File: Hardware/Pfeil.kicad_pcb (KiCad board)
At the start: 4 copper layers, 50 x 9 mm, 61 parts, among them IC1 2536030320001, IC2 nPM1300-CAAA-R, J1 Conn_01x01_Socket, J2 Conn_01x01_Socket, J3 TagConnect, U1 NRF52840-CKAA-R, U2 WSEN-PADS_2511020213301, U3 WSEN-PADS_2511020213301, X1 XTAL 32MHz 8pF, X2 XTAL 32.768kHz 9pF

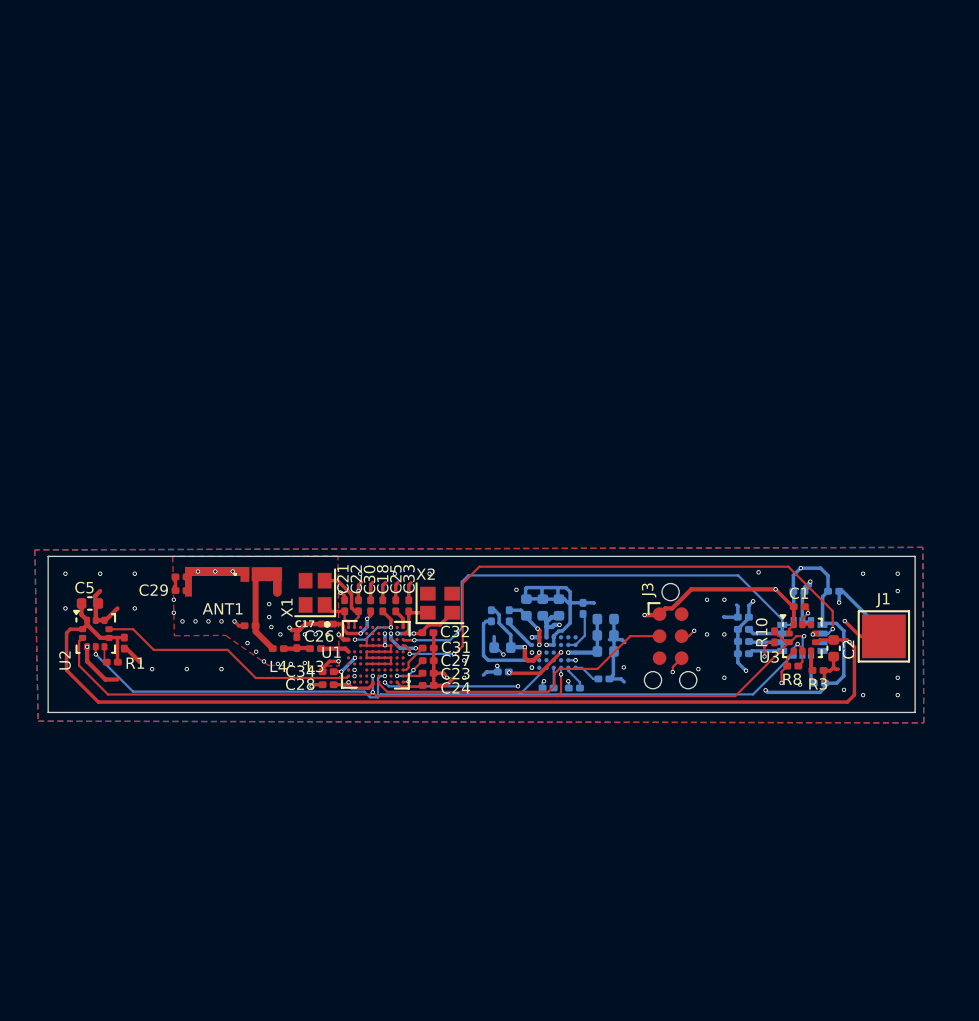
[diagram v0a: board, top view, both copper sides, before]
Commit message: nrf 52840 changing of the package
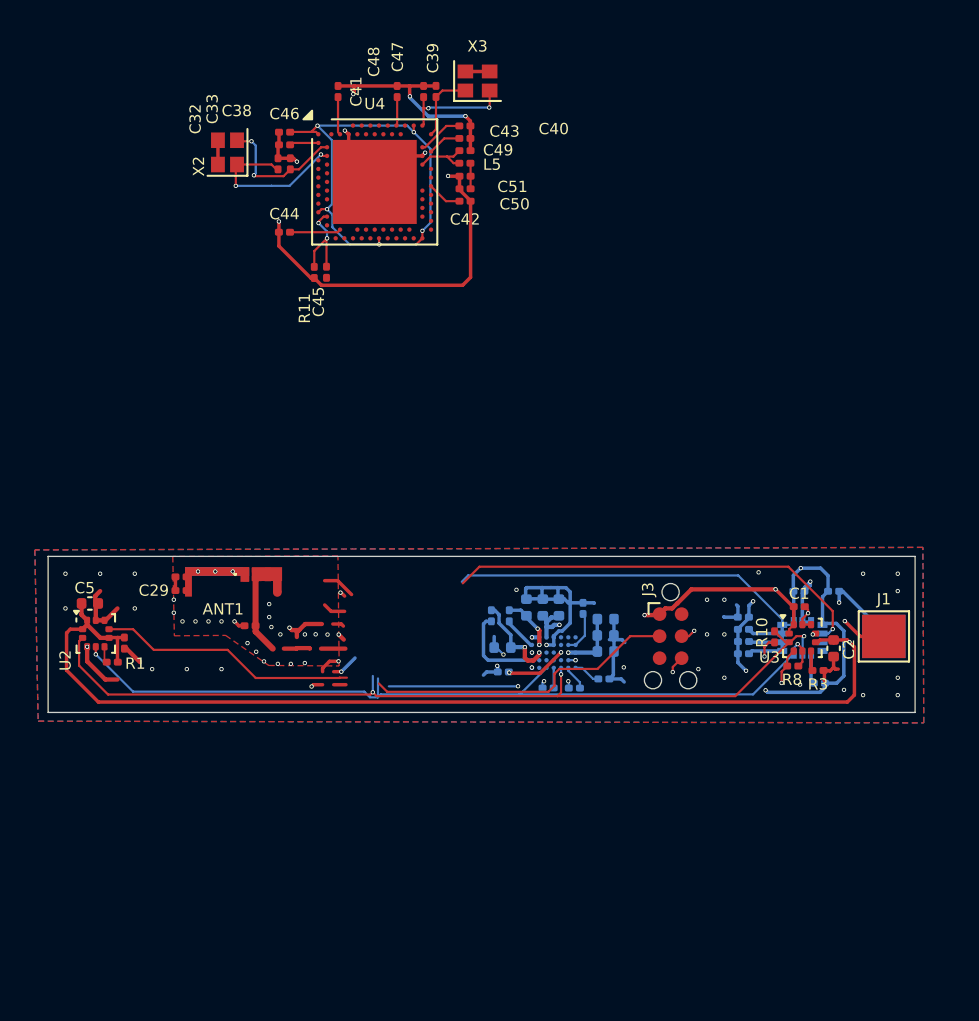
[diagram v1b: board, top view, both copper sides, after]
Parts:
- removed C17, C18: 1uF X7R 10%, Capacitor_SMD:C_0201_0603Metric
- removed C21, C22: 12pF NP0 2%, Capacitor_SMD:C_0201_0603Metric
- removed C23, C24, C31: 4.7uF X7R 10%, Capacitor_SMD:C_0201_0603Metric
- removed C25, C28, C30: 100nF X7R 10%, Capacitor_SMD:C_0201_0603Metric
- removed C26: 1pF 5% 0201, Capacitor_SMD:C_0201_0603Metric
- removed C27: 4.7uF X7S 10%, Capacitor_SMD:C_0201_0603Metric
- removed C34: 820pF X7R 10%, Capacitor_SMD:C_0201_0603Metric
- removed L3: 3.9nH 0201 5%, Inductor_SMD:L_0201_0603Metric
- removed L4: 4.7nH 0201 5%, Inductor_SMD:L_0201_0603Metric
- removed U1: NRF52840-CKAA-R, NRF52840-CKAA-R:BGA94C35P10X10_360X354X51N
- removed X1: XTAL 32MHz 8pF, Crystal:Crystal_SMD_2016-4Pin_2.0x1.6mm
- added C38: 100nF, Capacitor_SMD:C_0201_0603Metric, F.Cu at (138.6, 28.3)
- added C39: N.C., Capacitor_SMD:C_0201_0603Metric, F.Cu at (145.1, 25.2)
- added C40: 100pF, Capacitor_SMD:C_0201_0603Metric, F.Cu at (149.0, 27.2)
- added C41: 1pF, Capacitor_SMD:C_0201_0603Metric, F.Cu at (141.7, 25.2)
- added C42: 820pF, Capacitor_SMD:C_0201_0603Metric, F.Cu at (149.0, 31.5)
- added C43: N.C., Capacitor_SMD:C_0201_0603Metric, F.Cu at (149.0, 27.9)
- added C44: 4.7uF, Capacitor_SMD:C_0201_0603Metric, F.Cu at (138.6, 33.3)
- added C45: 820pF, Capacitor_SMD:C_0201_0603Metric, F.Cu at (140.3, 35.6)
- added C46: 4.7uF, Capacitor_SMD:C_0201_0603Metric, F.Cu at (138.6, 27.5)
- added C47: 12pF NP0 2%, Capacitor_SMD:C_0201_0603Metric, F.Cu at (147.4, 25.2)
- added C48: 12pF NP0 2%, Capacitor_SMD:C_0201_0603Metric, F.Cu at (146.7, 25.2)
- added C49: 100nF, Capacitor_SMD:C_0201_0603Metric, F.Cu at (149.0, 28.6)
- added C50: 100nF, Capacitor_SMD:C_0201_0603Metric, F.Cu at (149.0, 30.8)
- added C51: 100nF, Capacitor_SMD:C_0201_0603Metric, F.Cu at (149.0, 30.1)
- added L5: L, Inductor_SMD:L_0201_0603Metric, F.Cu at (149.0, 29.3)
- added R11: 2R2, Resistor_SMD:R_0201_0603Metric, F.Cu at (141.1, 35.6)
- added U4: nRF52840, Package_DFN_QFN:Nordic_AQFN-73-1EP_7x7mm_P0.5mm, F.Cu at (143.8, 30.4)
- added X3: XTAL 32MHz 8pF, Crystal:Crystal_SMD_2016-4Pin_2.0x1.6mm, F.Cu at (149.8, 24.6)
- moved X2 28.7 mm to (135.3, 28.7), turned to 90 degrees
- moved C32 28.4 mm to (138.3, 29.4), turned to 90 degrees
- moved C33 26.4 mm to (139.0, 29.4)
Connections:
- net VDD renamed /ISDS_INT_00
- C32 pad 1: Net-(U1A-P0.00/XL1) -> Net-(U4-XL2/P0.01)
- C33 pad 2: Net-(U1A-P0.01/XL2) -> Net-(U4-XL1/P0.00)
- X2 pad 1: Net-(U1A-P0.01/XL2) -> Net-(U4-XL2/P0.01)
- X2 pad 2: Net-(U1A-P0.00/XL1) -> Net-(U4-XL1/P0.00)
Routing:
- net GND: track 93.8 -> 123.3 mm, vias 73 -> 71
- net GND VDD NRF: track 0.00 -> 28.1 mm, vias 0 -> 5
- net /ISDS_INT_00: track 99.2 -> 72.4 mm, vias 10 -> 4
- net /SWCLK: track 27.5 -> 16.7 mm, vias 2 -> 1
- net (no net): track 0.00 -> 10.5 mm, vias 0 -> 1
- net Net-(U4-XL2/P0.01): track 0.00 -> 9.43 mm, vias 0 -> 2
- net Net-(U4-XL1/P0.00): track 0.00 -> 7.89 mm, vias 0 -> 2
- net /ISDS_INT_01: track 32.1 -> 24.5 mm, vias 3 -> 1
- net Net-(U4-XC2): track 0.00 -> 6.47 mm, vias 0 -> 2
- net GND VBUS NRF: track 0.00 -> 5.37 mm, vias 0 -> 2
- net Net-(U1C-XC2): track 4.16 -> 0.00 mm
- net Net-(U4-XC1): track 0.00 -> 4.12 mm
- net Net-(U1A-P0.00/XL1): track 3.69 -> 0.00 mm, vias 2 -> 0
- net Net-(U1B-DEC4): track 3.58 -> 0.00 mm, vias 2 -> 0
- net Net-(U4-ANT): track 0.00 -> 3.33 mm
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
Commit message: bigger pcb and no more npm1300
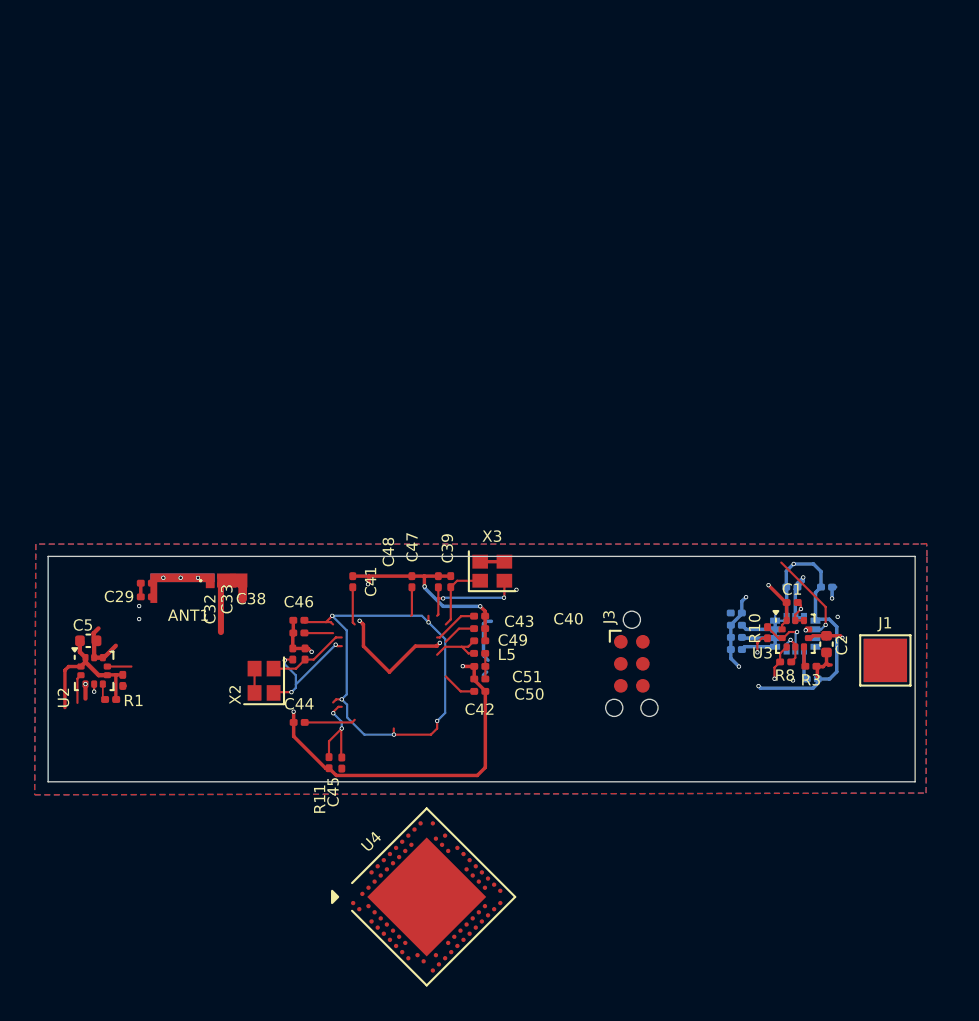
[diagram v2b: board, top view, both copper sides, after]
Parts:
- removed C10: 1.0uF, Capacitor_SMD:C_0201_0603Metric
- removed C11: 1.0uF X5R 10V 10%, Capacitor_SMD:C_0201_0603Metric
- removed C12, C13, C14, C15, C16, C19, C36: 10uF X5R 25V 20%, Capacitor_SMD:C_0402_1005Metric
- removed C37: 100nF X5R 10%, Capacitor_SMD:C_0201_0603Metric
- removed C6: 0.8pF NPO 5%, Capacitor_SMD:C_0201_0603Metric
- removed IC2: nPM1300-CAAA-R, nPM1300-CAAA-R:BGA35C44P7X5_308X238X51
- removed L1, L2: 2.2uH DCR <400mR 20%, Inductor_SMD:L_0201_0603Metric
- removed R12: 47k 1%, Resistor_SMD:R_0201_0603Metric
- removed R13: 270k 1%, Resistor_SMD:R_0201_0603Metric
- moved U4 41.3 mm to (146.8, 71.6), turned to 45 degrees
- moved X2 30.5 mm to (137.5, 59.2)
- moved R11 28.3 mm to (141.9, 63.9)
- moved C32 28.3 mm to (139.1, 57.6)
- moved C50 28.3 mm to (149.9, 59.1)
- moved C51 28.3 mm to (149.9, 58.3)
- moved C33 28.3 mm to (139.8, 57.6)
- moved C42 28.3 mm to (149.9, 59.8)
- moved C44 28.3 mm to (139.5, 61.6)
- moved C45 28.3 mm to (141.2, 63.9)
- moved X3 28.3 mm to (150.6, 52.9)
- moved C39 28.3 mm to (146.0, 53.5)
- moved C40 28.3 mm to (149.9, 55.4)
- moved C41 28.3 mm to (142.6, 53.5)
- moved C43 28.3 mm to (149.9, 56.2)
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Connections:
- C46 pad 2: GND VDD NRF -> GND
- R11 pad 2: GND VBUS -> GND
- U4 pad A22: GND VDD NRF -> GND
- U4 pad AD14: GND VDD NRF -> GND
- U4 pad AD23: GND VDD NRF -> GND
- U4 pad B1: GND VDD NRF -> GND
- U4 pad W1: GND VDD NRF -> GND
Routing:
- net /I2C_SCL: track 98.8 -> 7.42 mm, vias 5 -> 3
- net +3V3: track 88.9 -> 22.7 mm, vias 4 -> 2
- net /ISDS_INT_00: track 72.4 -> 35.3 mm
- net GND VDD NRF: track 28.1 -> 0.00 mm, vias 5 -> 0
- net /PADS_INT02: track 26.0 -> 3.63 mm, vias 2 -> 1
- net /SWDIO: track 20.0 -> 0.00 mm, vias 1 -> 0
- net /VBAT: track 19.5 -> 0.00 mm, vias 2 -> 0
- net /RESET: track 18.1 -> 0.00 mm
- net /ISDS_INT_01: track 24.5 -> 6.75 mm
- net /SWCLK: track 16.7 -> 0.00 mm, vias 1 -> 0
- net /PADS_INT01: track 14.9 -> 1.39 mm
- net GND: track 123.3 -> 113.6 mm, vias 71 -> 24
- net (no net): track 10.5 -> 1.40 mm, vias 1 -> 0
- net Net-(IC2-PVDD): track 6.12 -> 0.00 mm, vias 2 -> 0
- net /3.0V: track 5.45 -> 0.00 mm, vias 2 -> 0
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- added copper zone on B.Cu, net (none)
- added copper zone on F.Cu, net (none)
- added copper zone on In1.Cu, net (none)
- added copper zone on In2.Cu, net (none)
- removed copper zone on B.Cu, net GND
- removed copper zone on F.Cu, net GND
- removed copper zone on In1.Cu, net GND
- removed copper zone on In2.Cu, net GND
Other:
- board size 50 x 9 mm -> 50 x 13 mm

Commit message: start ing to routing with the new pcb
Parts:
- removed J1, J2: Conn_01x01_Socket, TestPoint:TestPoint_Pad_2.5x2.5mm
- added C10: 1uF, Capacitor_SMD:C_0201_0603Metric, F.Cu at (161.1, 61.8)
- added C11: 1uF, Capacitor_SMD:C_0201_0603Metric, F.Cu at (161.1, 62.5)
- added C12: 1uF, Capacitor_SMD:C_0201_0603Metric, F.Cu at (165.8, 61.4)
- added C6: 0.8pF NPO 5%, Capacitor_SMD:C_0201_0603Metric, F.Cu at (153.2, 56.2)
- added IC2: AP7312-1233FM-7, LIB_AP7312-1233FM-7:SON50P201X181X60-7N, F.Cu at (163.4, 62.0)
- moved ANT1 18.6 mm to (153.6, 53.5)
- moved C29 18.6 mm to (149.2, 54.4)
- moved C4 18.6 mm to (149.2, 53.6)
- moved NT1 18.6 mm to (154.8, 54.0)
- moved U4 15.1 mm to (139.3, 58.6)
- moved C48 10.4 mm to (137.1, 53.5), turned to 135 degrees
- moved C39 9.43 mm to (136.6, 54.0), turned to -45 degrees
- moved C41 8.80 mm to (134.2, 56.3), turned to -45 degrees
- moved X3 7.93 mm to (142.7, 53.8), turned to -45 degrees
- moved C47 7.17 mm to (141.1, 52.9), turned to 45 degrees
- moved C38 7.07 mm to (133.3, 59.9), turned to 45 degrees
- moved C33 6.44 mm to (134.2, 60.8), turned to 45 degrees
- moved C40 6.33 mm to (143.6, 55.4), turned to -135 degrees
- moved C42 6.29 mm to (144.6, 56.4), turned to -135 degrees
- moved X2 5.91 mm to (132.7, 62.7), turned to 135 degrees
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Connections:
- C50 pad 1: Net-(C50-Pad1) -> /FEEL
- C51 pad 1: Net-(C50-Pad1) -> /FEEL
- IC1 pad 13: /I2C_SCL -> /I2C_SCL 
- IC1 pad 14: /I2C_SCL -> /I2C_SDA
- L5 pad 1: Net-(C50-Pad1) -> /FEEL
- R8 pad 2: /I2C_SCL -> /I2C_SDA
- U2 pad 2: /I2C_SCL -> /I2C_SCL 
- U2 pad 4: /I2C_SCL -> /I2C_SDA 
- U3 pad 2: /I2C_SCL -> /I2C_SCL 
- U3 pad 4: /I2C_SCL -> /I2C_SDA 
- U4 pad AA24: unconnected-(U4-SWDCLK-PadAA24) -> /SWCLK
- U4 pad AC13: unconnected-(U4-P0.18/~{RESET}-PadAC13) -> /RESET
- U4 pad AC21: unconnected-(U4-P0.25-PadAC21) -> /I2C_SDA 
- U4 pad AC24: unconnected-(U4-SWDIO-PadAC24) -> /SWDIO
- U4 pad G1: unconnected-(U4-P0.26-PadG1) -> /I2C_SCL 
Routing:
- net /I2C_SDA : track 0.00 -> 26.5 mm, vias 0 -> 2
- net /ISDS_INT_00: track 35.3 -> 15.4 mm, vias 4 -> 0
- net GND: track 113.6 -> 95.5 mm, vias 24 -> 12
- net /SWDIO: track 0.00 -> 14.6 mm
- net /SWCLK: track 0.00 -> 14.5 mm
- net /RESET: track 0.00 -> 14.1 mm, vias 0 -> 2
- net /I2C_SCL : track 0.00 -> 12.0 mm, vias 0 -> 2
- net /I2C_SDA: track 0.00 -> 11.2 mm, vias 0 -> 3
- net /FEEL: track 4.47 -> 14.4 mm
- net +3V3: track 22.7 -> 13.2 mm, vias 2 -> 0
- net /I2C_SCL: track 7.42 -> 0.00 mm, vias 3 -> 0
- net /ISDS_INT_01: track 6.75 -> 0.00 mm, vias 1 -> 0
- net /PADS_INT02: track 3.63 -> 0.00 mm, vias 1 -> 0
- net /SW2: track 2.72 -> 0.00 mm
- net Net-(U4-XL2/P0.01): track 7.36 -> 4.93 mm, vias 3 -> 0
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
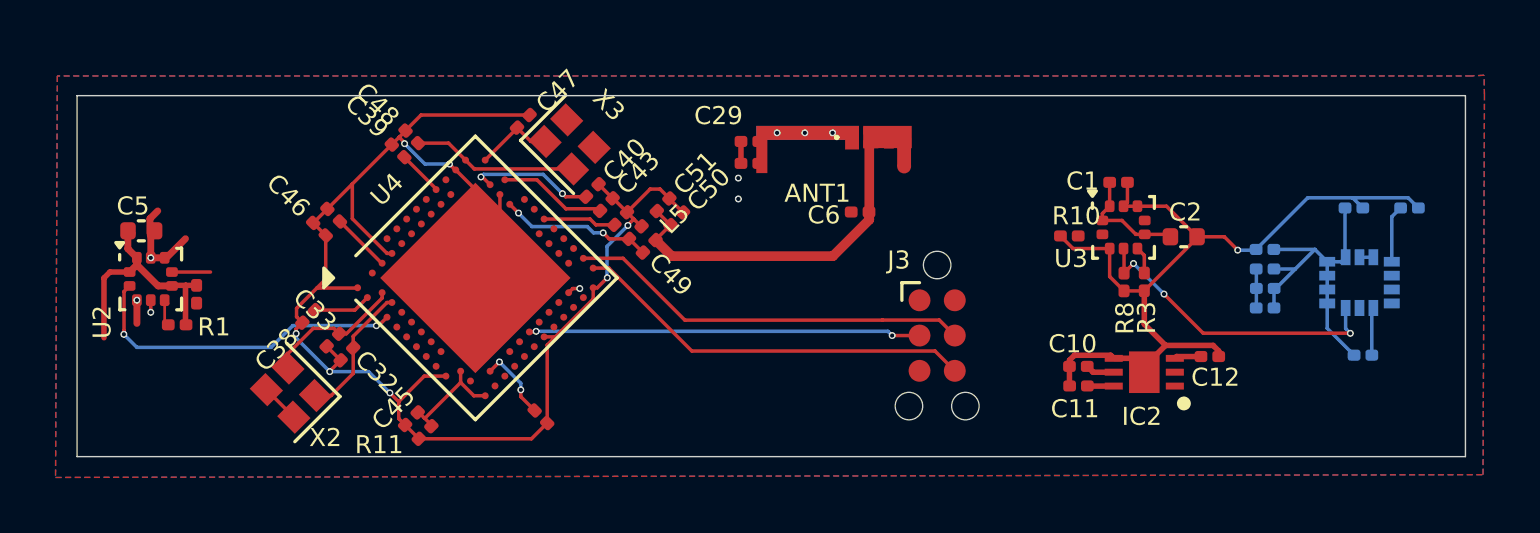
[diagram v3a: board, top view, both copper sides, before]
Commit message: Routing and evry component is on the front
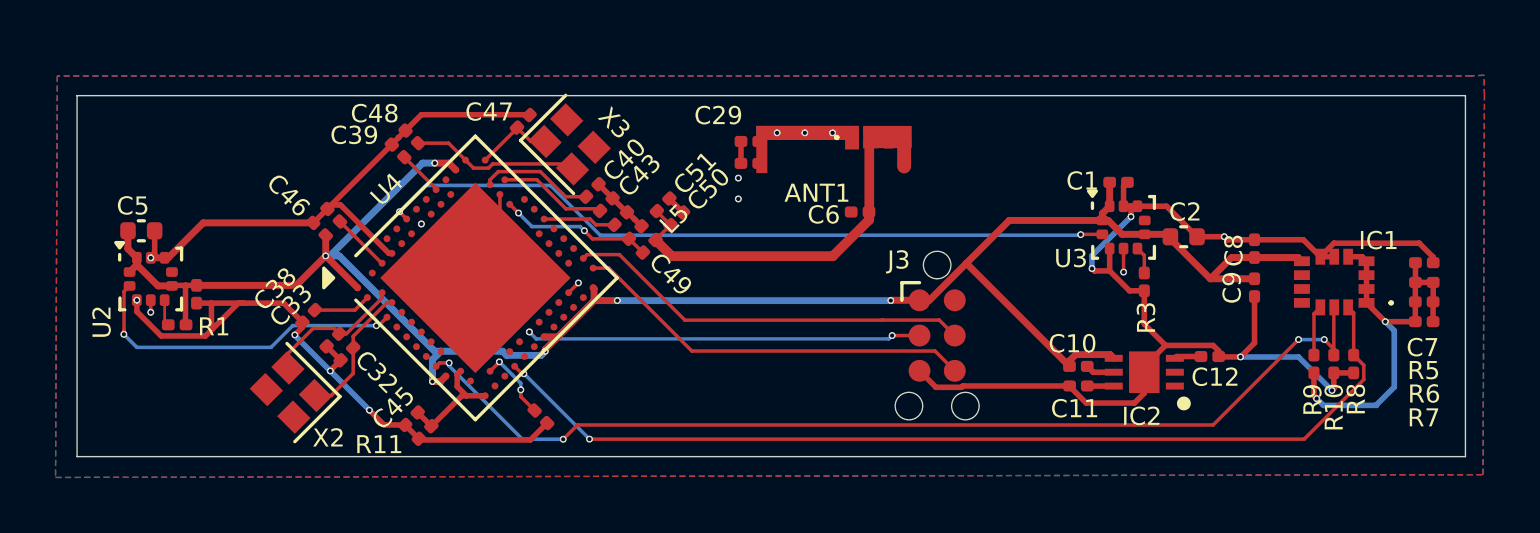
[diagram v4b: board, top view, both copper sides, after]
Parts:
- C7, C8, C9, IC1, R5, R6, R7, R9: moved to F.Cu
- moved R10 10.6 mm to (170.3, 61.7), turned to 90 degrees
- moved R8 8.78 mm to (171.0, 61.7)
- moved C8 5.77 mm to (167.4, 57.5), turned to 90 degrees
- moved C7 5.76 mm to (173.5, 58.0), turned to 0 degrees
- moved R5 5.76 mm to (173.5, 58.7), turned to 180 degrees
- moved R7 5.75 mm to (173.5, 60.1), turned to 180 degrees
- moved R6 5.75 mm to (173.5, 59.4), turned to 180 degrees
- moved C9 4.59 mm to (167.4, 58.9), turned to -90 degrees
- moved R9 1.79 mm to (169.5, 61.7), turned to -90 degrees
- moved IC1 0.91 mm to (170.3, 58.7), turned to 180 degrees
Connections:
- C10 pad 2: GND -> +3V3
- C46 pad 2: GND -> +3V3
- C8 pad 1: /ISDS_INT_00 -> +3V3
- C9 pad 1: /ISDS_INT_00 -> +3V3
- IC1 pad 8: /ISDS_INT_00 -> +3V3
- IC2 pad 4: GND -> +3V3
- R10 pad 2: /I2C_SCL -> /I2C_SCL 
- U2 pad 2: /I2C_SCL  -> /I2C_SCL A1
- U2 pad 4: /I2C_SDA  -> /I2C_SDA A1
- U3 pad 2: /I2C_SCL  -> /I2C_SCL A2
- U3 pad 4: /I2C_SDA  -> /I2C_SDA A2
- U4 pad A12: unconnected-(U4-AIN0/P0.02-PadA12) -> /I2C_SCL A2
- U4 pad A22: GND -> +3V3
- U4 pad AC21: /I2C_SDA  -> /I2C_SDA A1
- U4 pad AD14: GND -> +3V3
- U4 pad AD23: GND -> +3V3
- U4 pad AD8: unconnected-(U4-P0.13-PadAD8) -> /I2C_SDA
- U4 pad B1: GND -> +3V3
- U4 pad B13: unconnected-(U4-AIN1/P0.03-PadB13) -> /I2C_SDA A2
- U4 pad G1: /I2C_SCL  -> /I2C_SCL A1
- U4 pad U1: unconnected-(U4-TRACEDATA1/P0.12-PadU1) -> /I2C_SCL 
- U4 pad W1: GND -> +3V3
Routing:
- net +3V3: track 13.2 -> 72.4 mm, vias 0 -> 6
- net /I2C_SDA A2: track 0.00 -> 30.3 mm, vias 0 -> 2
- net /I2C_SCL A2: track 0.00 -> 26.9 mm, vias 0 -> 2
- net /I2C_SDA : track 26.5 -> 0.00 mm, vias 2 -> 0
- net /I2C_SCL : track 12.0 -> 37.2 mm, vias 2 -> 4
- net /I2C_SDA A1: track 0.00 -> 25.0 mm, vias 0 -> 2
- net /I2C_SDA: track 11.2 -> 35.4 mm, vias 3 -> 2
- net /I2C_SCL A1: track 0.00 -> 12.0 mm, vias 0 -> 2
- net (no net): track 1.40 -> 0.00 mm
- net /PADS_INT01: track 1.39 -> 0.00 mm
- net GND: track 95.5 -> 94.9 mm
- net Net-(U4-DEC3): track 4.60 -> 4.13 mm, vias 2 -> 0
- net /ISDS_INT_00: track 15.4 -> 15.1 mm, vias 0 -> 2
